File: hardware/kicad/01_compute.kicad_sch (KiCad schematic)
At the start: 0 parts

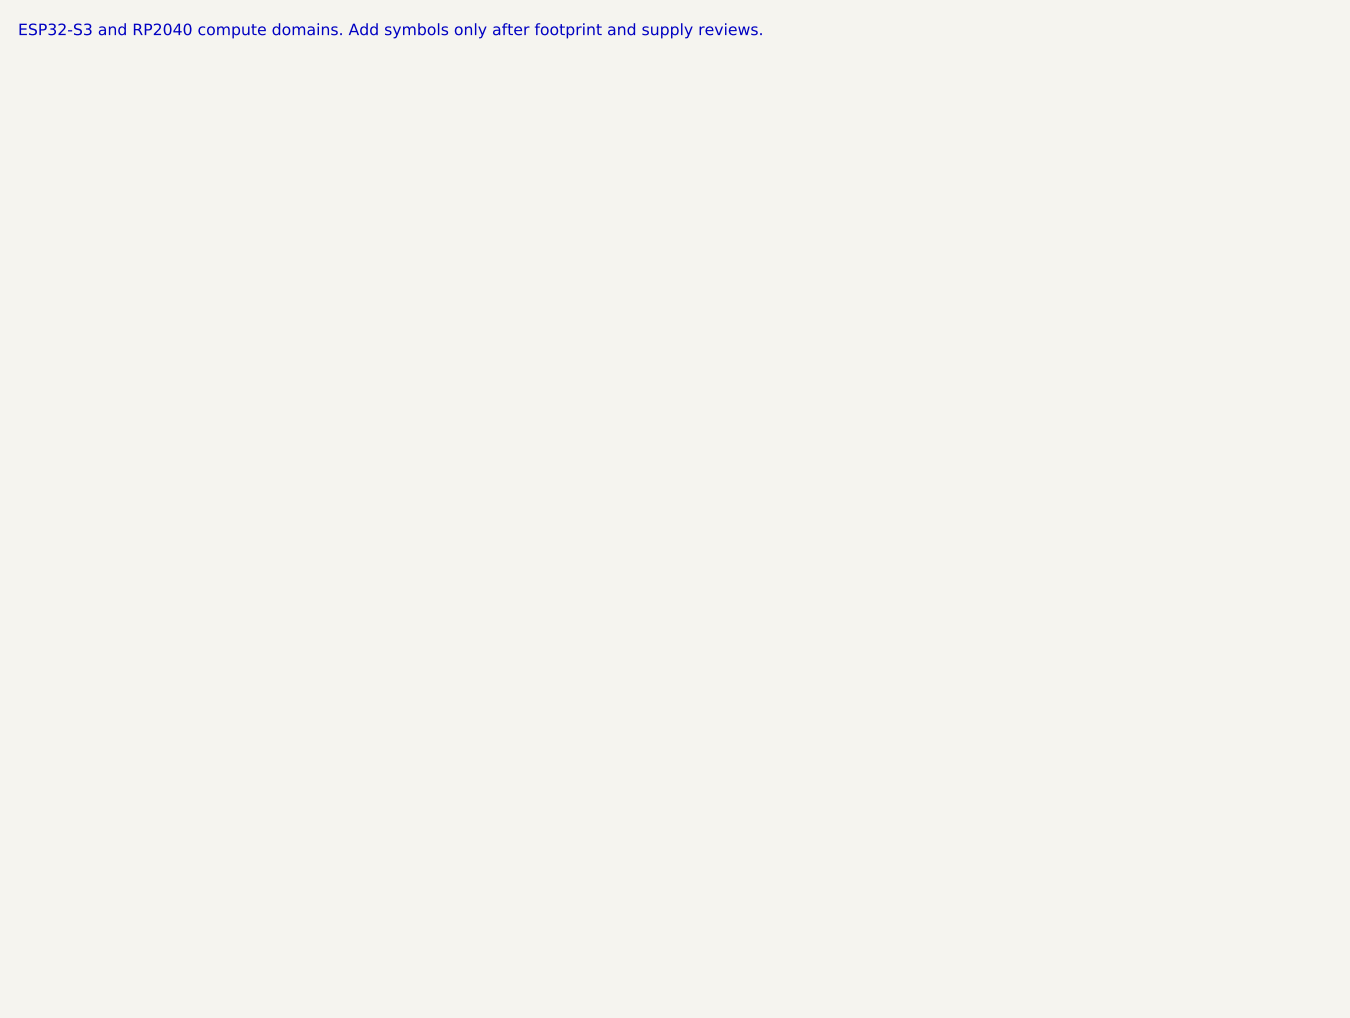
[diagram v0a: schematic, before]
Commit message: hardware: add reviewed ESP32 compute entry
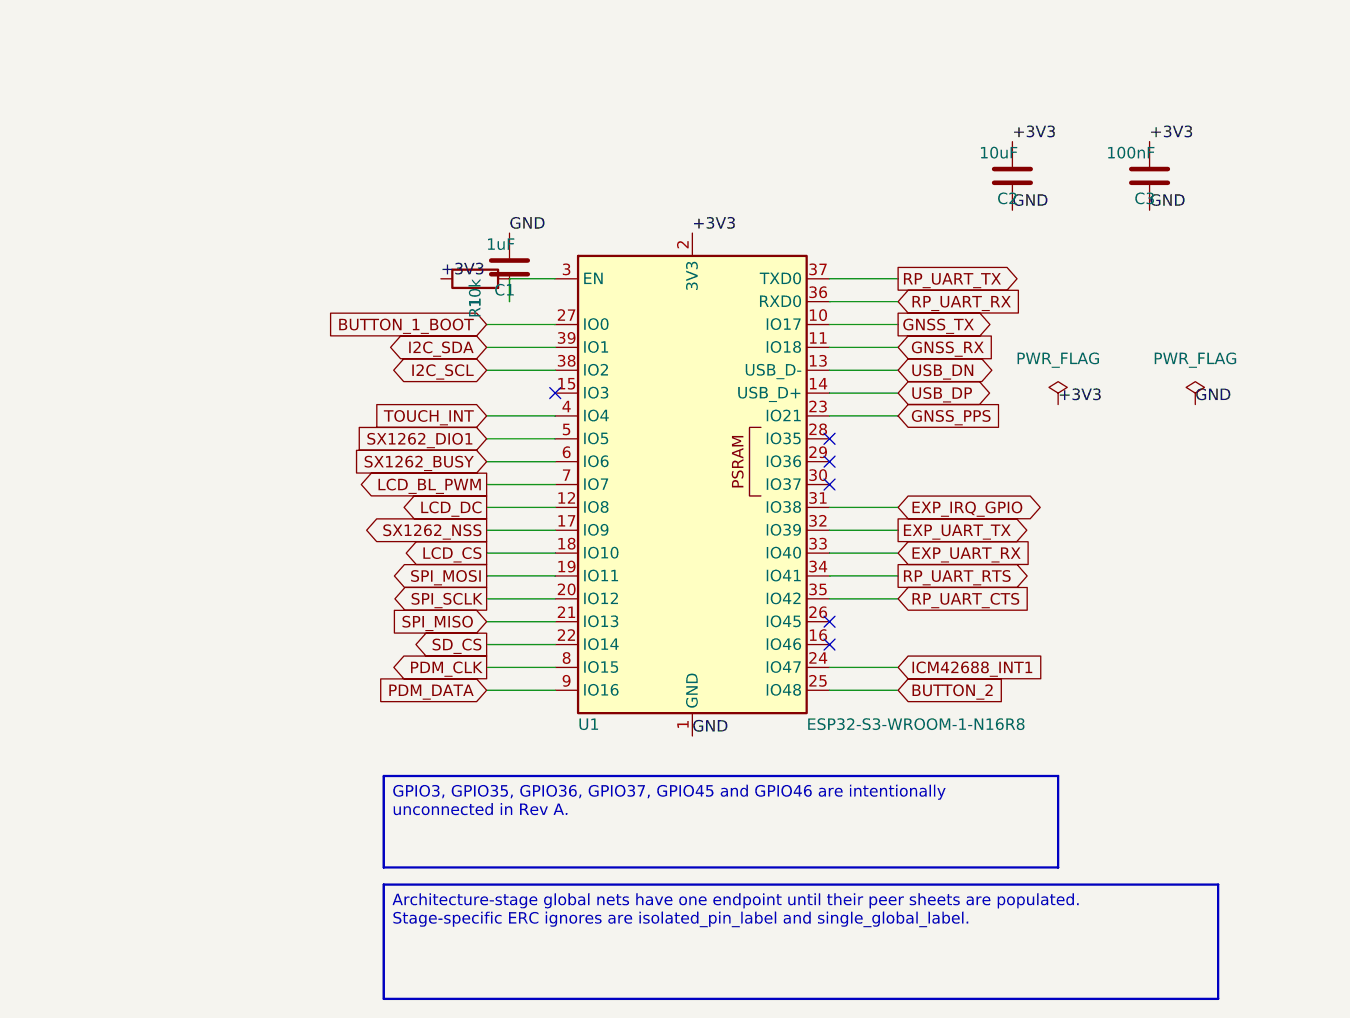
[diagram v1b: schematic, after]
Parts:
- added C1: 1uF, Capacitor_SMD:C_0603_1608Metric, symbol Device:C
- added C2: 10uF, Capacitor_SMD:C_0603_1608Metric, symbol Device:C
- added C3: 100nF, Capacitor_SMD:C_0603_1608Metric, symbol Device:C
- added R1: 10k, Resistor_SMD:R_0603_1608Metric, symbol Device:R
- added U1: ESP32-S3-WROOM-1-N16R8, RF_Module:ESP32-S3-WROOM-1, symbol RF_Module:ESP32-S3-WROOM-1
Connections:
- new net: C1.1, R1.2, U1.3 (EN)
- new net +3V3: C2.2, C3.2, R1.1, U1.2 (3V3)
- new net BUTTON_1_BOOT: U1.27 (IO0)
- new net BUTTON_2: U1.25 (IO48)
- new net EXP_IRQ_GPIO: U1.31 (IO38)
- new net EXP_UART_RX: U1.33 (IO40)
- new net EXP_UART_TX: U1.32 (IO39)
- new net GND: C1.2, C2.1, C3.1, U1.1 (GND), U1.40 (GND), U1.41 (GND)
- new net GNSS_PPS: U1.23 (IO21)
- new net GNSS_RX: U1.11 (IO18)
- new net GNSS_TX: U1.10 (IO17)
- new net I2C_SCL: U1.38 (IO2)
- new net I2C_SDA: U1.39 (IO1)
- new net ICM42688_INT1: U1.24 (IO47)
- new net LCD_BL_PWM: U1.7 (IO7)
- new net LCD_CS: U1.18 (IO10)
- new net LCD_DC: U1.12 (IO8)
- new net PDM_CLK: U1.8 (IO15)
- new net PDM_DATA: U1.9 (IO16)
- new net RP_UART_CTS: U1.35 (IO42)
- new net RP_UART_RTS: U1.34 (IO41)
- new net RP_UART_RX: U1.36 (RXD0)
- new net RP_UART_TX: U1.37 (TXD0)
- new net SD_CS: U1.22 (IO14)
- new net SPI_MISO: U1.21 (IO13)
- new net SPI_MOSI: U1.19 (IO11)
- new net SPI_SCLK: U1.20 (IO12)
- new net SX1262_BUSY: U1.6 (IO6)
- new net SX1262_DIO1: U1.5 (IO5)
- new net SX1262_NSS: U1.17 (IO9)
- new net TOUCH_INT: U1.4 (IO4)
- new net USB_DN: U1.13 (USB_D-)
- new net USB_DP: U1.14 (USB_D+)
- no-connect marks 0 -> 6
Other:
- note removed: "ESP32-S3 and RP2040 compute domains. Add symbols only after footprint and supply reviews."
- title: 01 Compute -> 01 Compute - ESP32-S3

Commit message: hardware: add reviewed sensor subset
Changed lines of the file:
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@@
 		)
 	)
-	(label "+3V3"
+	(global_label "+3V3"
+		(shape bidirectional)
 		(at 100.33 52.07 0.0000)
+		(fields_autoplaced yes)
 		(effects
 			(font
@@
 		)
 	)
-	(label "GND"
+	(global_label "GND"
+		(shape bidirectional)
 		(at 100.33 107.95 0.0000)
+		(fields_autoplaced yes)
 		(effects
 			(font
@@
 		)
 	)
-	(label "+3V3"
+	(global_label "+3V3"
+		(shape bidirectional)
 		(at 72.39 57.15 0.0000)
+		(fields_autoplaced yes)
 		(effects
 			(font
@@
 		)
 	)
-	(label "GND"
+	(global_label "GND"
+		(shape bidirectional)
 		(at 80.01 52.07 0.0000)
+		(fields_autoplaced yes)
 		(effects
 			(font
@@
 		)
 	)
-	(label "+3V3"
+	(global_label "+3V3"
+		(shape bidirectional)
 		(at 135.89 41.91 0.0000)
+		(fields_autoplaced yes)
 		(effects
 			(font
@@
 		)
 	)
-	(label "GND"
+	(global_label "GND"
+		(shape bidirectional)
 		(at 135.89 49.53 0.0000)
+		(fields_autoplaced yes)
 		(effects
 			(font
@@
 		)
 	)
-	(label "+3V3"
+	(global_label "+3V3"
+		(shape bidirectional)
 		(at 151.13 41.91 0.0000)
+		(fields_autoplaced yes)
 		(effects
 			(font
@@
 		)
 	)
-	(label "GND"
+	(global_label "GND"
+		(shape bidirectional)
 		(at 151.13 49.53 0.0000)
+		(fields_autoplaced yes)
 		(effects
 			(font
@@
 		)
 	)
-	(label "+3V3"
+	(global_label "+3V3"
+		(shape bidirectional)
 		(at 140.97 71.12 0.0000)
+		(fields_autoplaced yes)
 		(effects
 			(font
@@
 		)
 	)
-	(label "GND"
+	(global_label "GND"
+		(shape bidirectional)
 		(at 156.21 71.12 0.0000)
+		(fields_autoplaced yes)
 		(effects
 			(font
